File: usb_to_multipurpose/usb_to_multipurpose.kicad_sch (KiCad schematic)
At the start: 27 parts, among them P1 USB_C_Plug_USB2.0, U1 FT232H, U2 93LC56B, U3 PM2.54-1*11, U4 PM2.54-1*11, Y1 12MHz

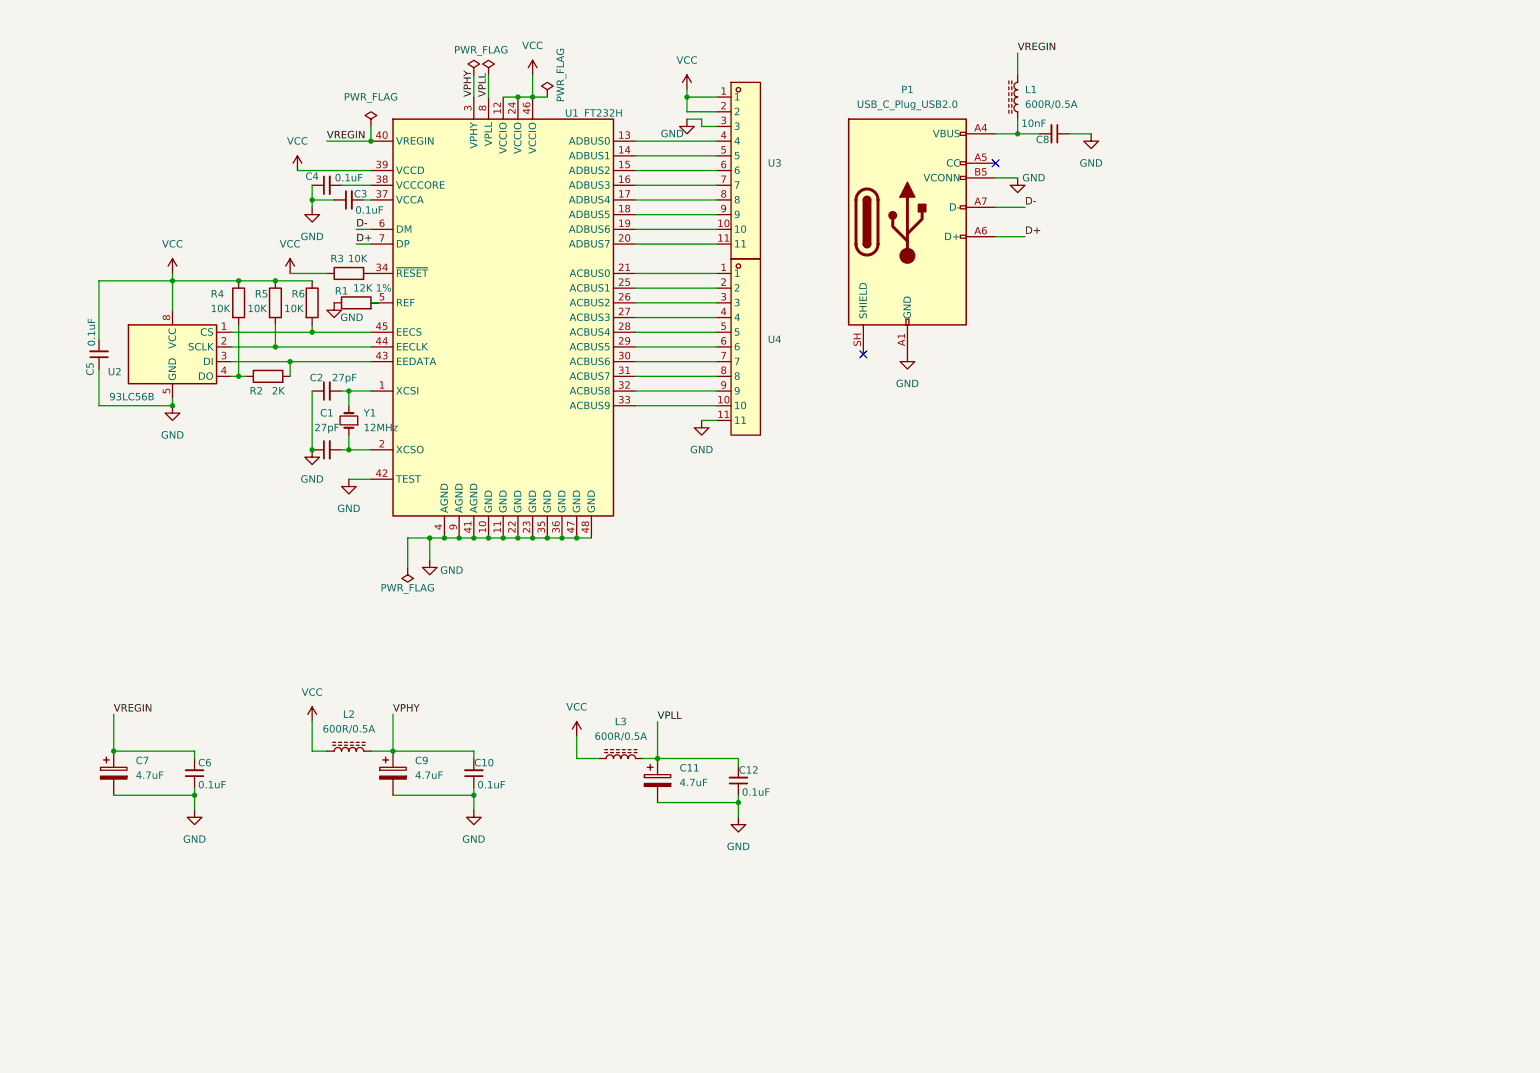
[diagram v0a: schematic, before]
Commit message: Update schematic for self-powered configuration running on 3.3V. Added footprints.
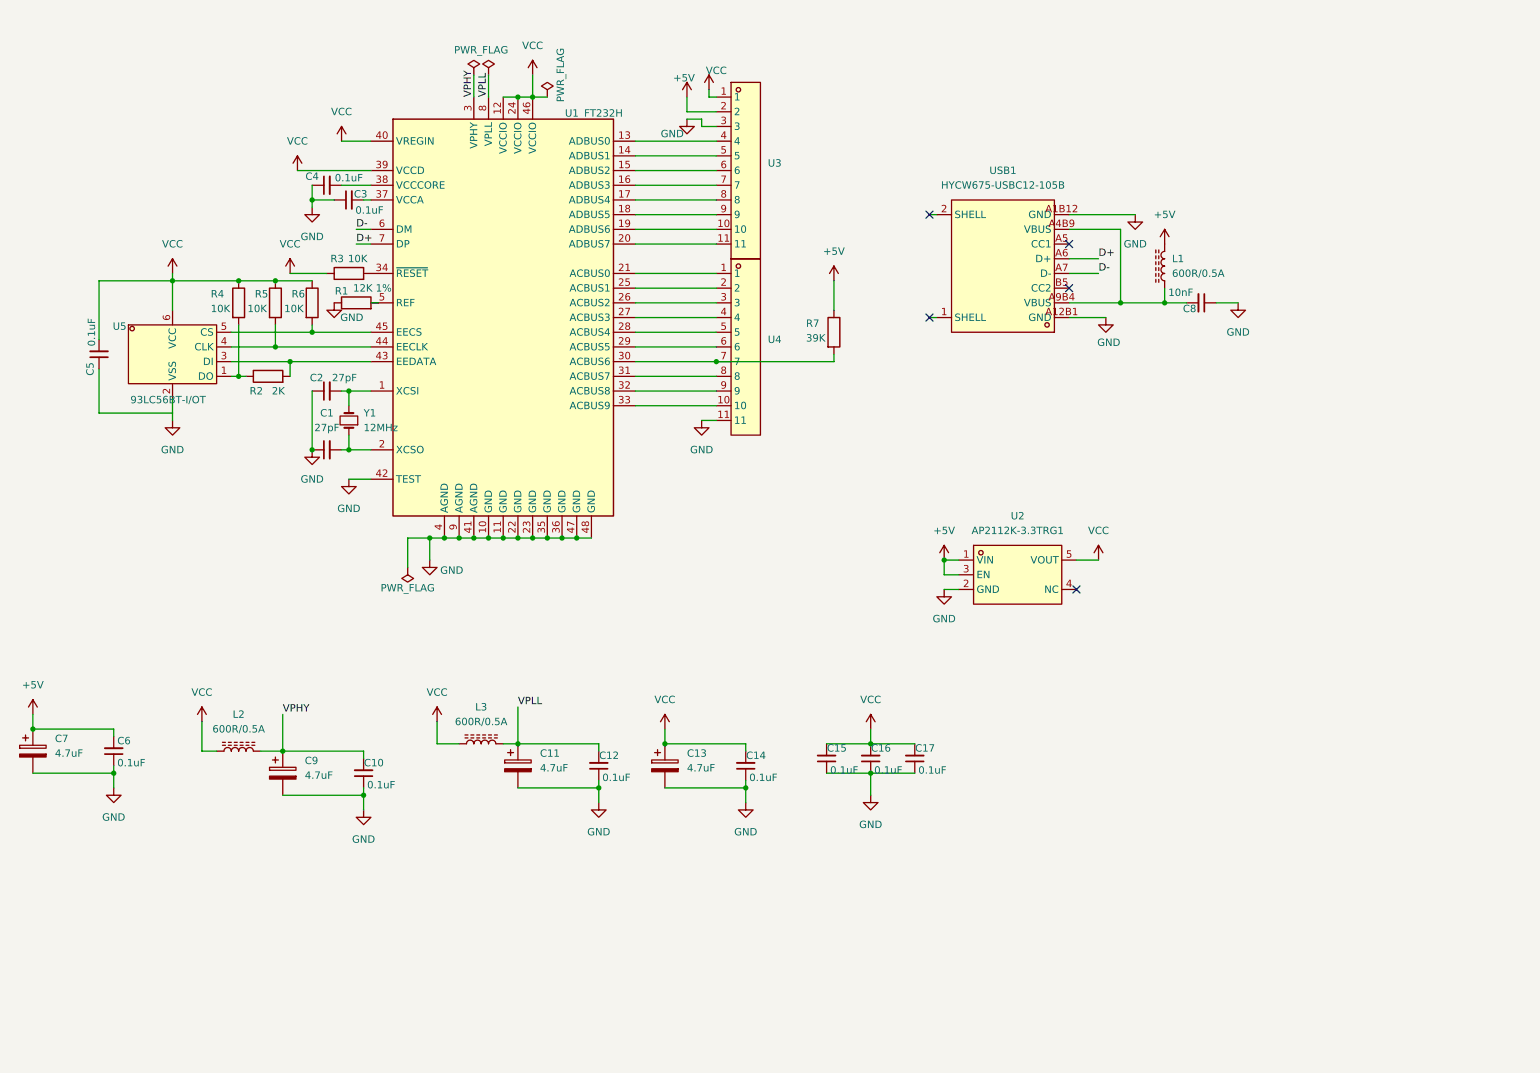
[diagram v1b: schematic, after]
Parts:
- removed P1: USB_C_Plug_USB2.0, symbol Connector:USB_C_Plug_USB2.0
- removed U2: 93LC56B, symbol Memory_EEPROM:93LCxxB
- added C13: 4.7uF, Capacitor_SMD:C_0603_1608Metric, symbol Device:C_Polarized
- added C14, C15, C16, C17: 0.1uF, Capacitor_SMD:C_0603_1608Metric, symbol Device:C_Small
- added R7: 39K, easyeda2kicad:R0402, symbol Device:R
- added U2: AP2112K-3.3TRG1, easyeda2kicad:SOT-23-5_L2.9-W1.6-P0.95-LS2.7-BR, symbol easyeda2kicad:AP2112K-3.3TRG1
- added U5: 93LC56BT-I/OT, easyeda2kicad:SOT-23-6_L2.9-W1.6-P0.95-LS2.8-BR, symbol easyeda2kicad:93LC56BT-I_OT
- added USB1: HYCW675-USBC12-105B, easyeda2kicad:USB-C-SMD_HYCW675-USBC12-105B, symbol easyeda2kicad:HYCW675-USBC12-105B
- L1, L2, L3: footprint (none) -> easyeda2kicad:L0805
- R1: footprint (none) -> easyeda2kicad:R0603
- R2, R3, R4, R5, R6: footprint (none) -> easyeda2kicad:R0402
- U1: footprint Package_DFN_QFN:QFN-48-1EP_8x8mm_P0.5mm_EP6.2x6.2mm -> easyeda2kicad:LQFP-48_L7.0-W7.0-P0.50-LS9.0-TL
- U3, U4: footprint Connector_TE-Connectivity:TE_440054-2_1x02_P2.00mm_Vertical -> easyeda2kicad:HDR-TH_11P-P2.54-V-F
- Y1: footprint Connector_TE-Connectivity:TE_440054-2_1x02_P2.00mm_Vertical -> easyeda2kicad:OSC-SMD_4P-L3.2-W2.5-BL
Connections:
- net D+: now also USB1.A6 (D+)
- net D-: now also USB1.A7 (D-)
- net GND: now also C13.2, C14.1, C15.1, C16.1, C17.1, U2.2 (GND), U5.2 (VSS), USB1.A12B1 (GND), USB1.A1B12 (GND); no longer C5.1
- net VCC: now also U1.40 (VREGIN), C13.1, C14.2, C15.2, C16.2, C17.2, U2.5 (VOUT), U5.6 (VCC); no longer U3.2
- net at U1.30 (ACBUS6), U4.7: now also R7.2
- net at R2.2, U1.43 (EEDATA): now also U5.3 (DI)
- net at R5.2, U1.44 (EECLK): now also U5.4 (CLK)
- net at R6.2, U1.45 (EECS): now also U5.5 (CS)
- net at C8.2, L1.1: now also USB1.A4B9 (VBUS), USB1.A9B4 (VBUS)
- net at R2.1, R4.2: now also U5.1 (DO)
- net VREGIN renamed +5V
- net +5V: now also U3.2, R7.1, U2.1 (VIN), U2.3 (EN); no longer U1.40 (VREGIN)
- no-connect marks 2 -> 5
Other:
- moved on the sheet: C10, C11, C12, C6, C7, C8, C9, L1, L2, L3

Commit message: Add 2*8 header. Schematic cleanup.
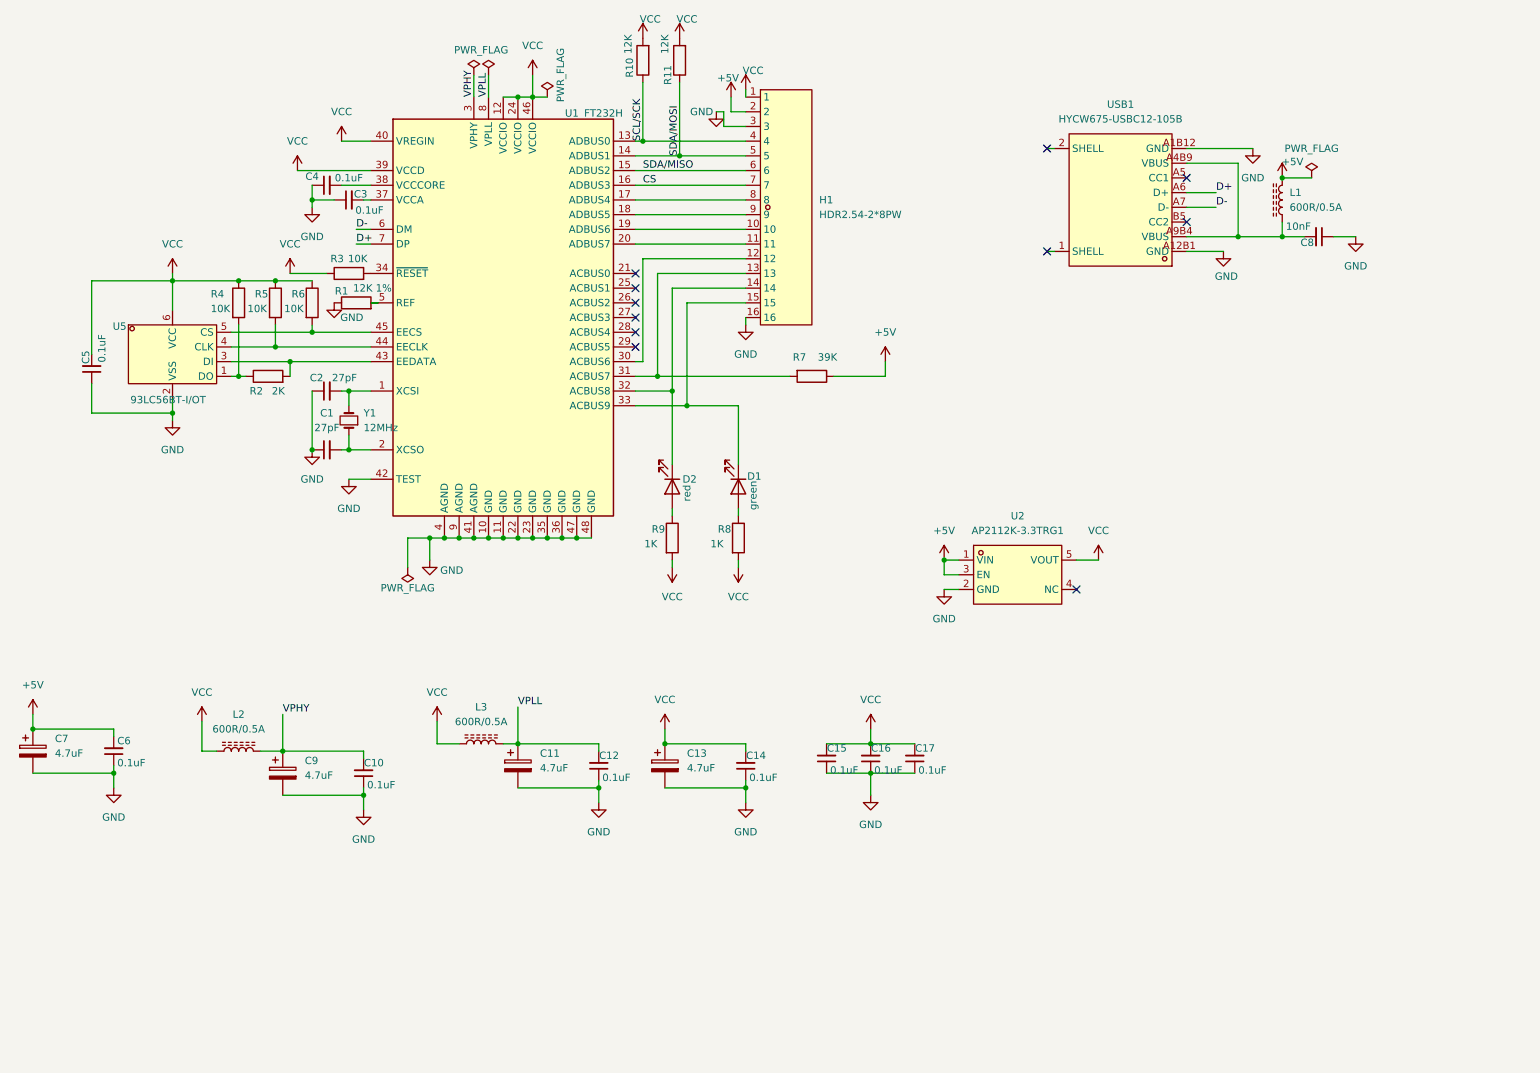
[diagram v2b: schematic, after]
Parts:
- removed U3, U4: PM2.54-1*11, easyeda2kicad:HDR-TH_11P-P2.54-V-F, symbol easyeda2kicad:PM2.54-1*11
- added D1: green, easyeda2kicad:LED0603-RD, symbol Device:LED
- added D2: red, easyeda2kicad:LED0603-RD, symbol Device:LED
- added H1: HDR2.54-2*8PW, easyeda2kicad:HDR-TH_16P-P2.54-H-F-R2-C8-S2.54-W10.0, symbol easyeda2kicad:HDR2.54-2*8PW
- added R10, R11: 12K, easyeda2kicad:R0603, symbol Device:R
- added R8, R9: 1K, easyeda2kicad:R0402, symbol Device:R
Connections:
- net +5V: now also H1.2
- net GND: now also C5.1, H1.16, H1.3
- net VCC: now also H1.1, R10.2, R11.2, R8.2, R9.2
- net SCL/SCK: now reaches U1.13 (ADBUS0)
- net SCL/SCK: now also H1.4, R10.1
- net SDA/MOSI: now reaches U1.14 (ADBUS1)
- net SDA/MOSI: now also H1.5, R11.1
- net SDA/MISO: now reaches U1.15 (ADBUS2)
- net SDA/MISO: now also H1.6
- net CS: now reaches U1.16 (ADBUS3)
- net CS: now also H1.7
- net at U1.17 (ADBUS4): now also H1.8
- net at U1.18 (ADBUS5): now also H1.9
- net at U1.19 (ADBUS6): now also H1.10
- net at U1.20 (ADBUS7): now also H1.11
- net at U1.30 (ACBUS6): now also H1.12; no longer R7.2
- net at U1.31 (ACBUS7): now also R7.2, H1.13
- net at U1.32 (ACBUS8): now also D2.1 (K), H1.14
- net at U1.33 (ACBUS9): now also D1.1 (K), H1.15
- new net: D2.2 (A), R9.1
- new net: D1.2 (A), R8.1
- no-connect marks 5 -> 11
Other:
- moved on the sheet: C8, L1, R7, USB1

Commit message: Schematic refinements. Add schematic info.
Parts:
- removed C13, C7: 4.7uF, Capacitor_SMD:C_0603_1608Metric, symbol Device:C_Polarized
- removed C14, C5, C6: 0.1uF, Capacitor_SMD:C_0603_1608Metric, symbol Device:C_Small
- removed R6: 10K, easyeda2kicad:R0402, symbol Device:R
- R4, R5: value 10K -> 5K1; footprint easyeda2kicad:R0402 -> (none)
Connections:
- net +5V: now also U1.40 (VREGIN)
- net GND: now also R4.2, R5.2
- net VCC: no longer R4.1, R5.1, U1.40 (VREGIN)
- net at R2.1, U5.1 (DO): no longer R4.2
- net at U1.44 (EECLK), U5.4 (CLK): no longer R5.2
- net at U1.29 (ACBUS5): now also H1.12
- net at U1.30 (ACBUS6): now also H1.13; no longer H1.12
- net at R7.2, U1.31 (ACBUS7): no longer H1.13
- net at USB1.A5 (CC1): now also R4.1
- net at USB1.B5 (CC2): now also R5.1
- no-connect marks 11 -> 8
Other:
- title: (none) -> USB to multipurpose
- moved on the sheet: C15, C16, C17, C8, L1

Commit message: Prepare v1.0 of the PCB.
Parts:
- C1, C11, C2, C9: footprint Capacitor_SMD:C_0603_1608Metric -> easyeda2kicad:C0402
- C10, C12, C15, C16, C17, C3, C4, C8: footprint Capacitor_SMD:C_0603_1608Metric -> easyeda2kicad:C0201
- R4, R5: footprint (none) -> easyeda2kicad:R0402
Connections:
- net GND: now also USB1.1 (SHELL), USB1.2 (SHELL)
- net at U1.18 (ADBUS5): now also H1.10; no longer H1.9
- net at U1.19 (ADBUS6): now also H1.9; no longer H1.10
- no-connect marks 8 -> 6
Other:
- note added: "v1.0"
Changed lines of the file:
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@@
 		(date "2026-09-06")
 	)
+	(text "v1.0"
+		(exclude_from_sim no)
+		(at 270.51 193.548 0)
+		(effects
+			(font
+				(size 1.27 1.27)
+			)
+		)
+	)
+	(text ""
+		(exclude_from_sim no)
+		(at 188.976 173.99 0)
+		(effects
+			(font
+				(size 2.54 2.54)
+			)
+		)
+	)
 	(junction
 		(at 134.62 38.1)
@@
 	)
 	(junction
+		(at 194.31 54.61)
+		(diameter 0)
+		(color 0 0 0 0)
+	)
+	(junction
 		(at 106.68 27.94)
 		(diameter 0)
@@
 	)
 	(no_connect
-		(at 198.12 54.61)
-	)
-	(no_connect
 		(at 127 66.04)
 	)
@@
 	)
 	(no_connect
-		(at 198.12 36.83)
-	)
-	(no_connect
 		(at 127 68.58)
 	)
@@
 	(wire
 		(pts
-			(xy 104.14 139.7) (xy 106.68 139.7)
+			(xy 194.31 54.61) (xy 199.39 54.61)
 		)
 		(stroke
@@
 	(wire
 		(pts
-			(xy 111.76 104.14) (xy 109.22 104.14)
+			(xy 104.14 139.7) (xy 106.68 139.7)
 		)
 		(stroke
@@
 	(wire
 		(pts
-			(xy 78.74 50.8) (xy 81.28 50.8)
+			(xy 111.76 104.14) (xy 109.22 104.14)
 		)
 		(stroke
@@
 	(wire
 		(pts
-			(xy 135.89 81.28) (xy 135.89 63.5)
+			(xy 78.74 50.8) (xy 81.28 50.8)
 		)
 		(stroke
@@
 	(wire
 		(pts
-			(xy 144.78 107.95) (xy 144.78 109.22)
+			(xy 135.89 81.28) (xy 135.89 63.5)
 		)
 		(stroke
@@
 	(wire
 		(pts
-			(xy 198.12 54.61) (xy 199.39 54.61)
+			(xy 144.78 107.95) (xy 144.78 109.22)
 		)
 		(stroke
@@
 	(wire
 		(pts
-			(xy 127 48.26) (xy 146.05 48.26)
-		)
-		(stroke
-			(width 0)
-			(type default)
-		)
-	)
-	(wire
-		(pts
 			(xy 78.74 53.34) (xy 81.28 53.34)
 		)
@@
 	(wire
 		(pts
+			(xy 127 48.26) (xy 137.16 48.26)
+		)
+		(stroke
+			(width 0)
+			(type default)
+		)
+	)
+	(wire
+		(pts
 			(xy 144.78 81.28) (xy 135.89 81.28)
 		)
@@
 	(wire
 		(pts
+			(xy 127 50.8) (xy 127 49.53)
+		)
+		(stroke
+			(width 0)
+			(type default)
+		)
+	)
+	(wire
+		(pts
 			(xy 71.12 78.74) (xy 71.12 88.9)
 		)
@@
 	(wire
 		(pts
-			(xy 127 50.8) (xy 146.05 50.8)
+			(xy 143.51 27.94) (xy 143.51 30.48)
 		)
 		(stroke
@@
 	(wire
 		(pts
-			(xy 143.51 27.94) (xy 143.51 30.48)
+			(xy 93.98 104.14) (xy 91.44 104.14)
 		)
 		(stroke
@@
 	(wire
 		(pts
-			(xy 93.98 104.14) (xy 91.44 104.14)
+			(xy 203.2 107.95) (xy 207.01 107.95)
 		)
 		(stroke
@@
 	(wire
 		(pts
-			(xy 203.2 107.95) (xy 207.01 107.95)
+			(xy 222.25 44.45) (xy 224.79 44.45)
 		)
 		(stroke
@@
 	(wire
 		(pts
-			(xy 222.25 44.45) (xy 224.79 44.45)
+			(xy 137.16 48.26) (xy 137.16 50.8)
 		)
 		(stroke
@@
 	(wire
 		(pts
+			(xy 194.31 36.83) (xy 199.39 36.83)
+		)
+		(stroke
+			(width 0)
+			(type default)
+		)
+	)
+	(wire
+		(pts
 			(xy 246.38 41.91) (xy 251.46 41.91)
 		)
@@
 	(wire
 		(pts
-			(xy 198.12 36.83) (xy 199.39 36.83)
+			(xy 246.38 49.53) (xy 246.38 52.07)
 		)
 		(stroke
@@
 	(wire
 		(pts
-			(xy 246.38 49.53) (xy 246.38 52.07)
+			(xy 130.81 58.42) (xy 130.81 73.66)
 		)
 		(stroke
@@
 	(wire
 		(pts
-			(xy 130.81 58.42) (xy 130.81 73.66)
+			(xy 120.65 140.97) (xy 120.65 139.7)
 		)
 		(stroke
@@
 	(wire
 		(pts
-			(xy 120.65 140.97) (xy 120.65 139.7)
+			(xy 194.31 36.83) (xy 194.31 54.61)
 		)
 		(stroke
@@
 	(wire
 		(pts
+			(xy 146.05 49.53) (xy 146.05 48.26)
+		)
+		(stroke
+			(width 0)
+			(type default)
+		)
+	)
+	(wire
+		(pts
 			(xy 128.27 35.56) (xy 146.05 35.56)
 		)
@@
 	(wire
 		(pts
+			(xy 137.16 50.8) (xy 146.05 50.8)
+		)
+		(stroke
+			(width 0)
+			(type default)
+		)
+	)
+	(wire
+		(pts
 			(xy 134.62 38.1) (xy 134.62 25.4)
 		)
@@
 	(wire
 		(pts
+			(xy 127 49.53) (xy 146.05 49.53)
+		)
+		(stroke
+			(width 0)
+			(type default)
+		)
+	)
+	(wire
+		(pts
 			(xy 96.52 104.14) (xy 93.98 104.14)
 		)
@@
 			)
 		)
-		(property "Footprint" "Capacitor_SMD:C_0603_1608Metric"
+		(property "Footprint" "easyeda2kicad:C0201"
 			(at 120.65 143.51 0)
 			(hide yes)
@@
 	(symbol
 		(lib_id "power:GND")
+		(at 194.31 54.61 0)
+		(unit 1)
+		(body_style 1)
+		(exclude_from_sim no)
+		(in_bom yes)
+		(on_board yes)
+		(in_pos_files yes)
+		(dnp no)
+		(property "Reference" "#PWR027"
+			(at 194.31 60.96 0)
+			(hide yes)
+			(show_name no)
+			(do_not_autoplace no)
+			(effects
+				(font
+					(size 1.27 1.27)
+				)
+			)
+		)
+		(property "Value" "GND"
+			(at 194.818 58.928 0)
+			(show_name no)
+			(do_not_autoplace no)
+			(effects
+				(font
+					(size 1.27 1.27)
+				)
+			)
+		)
+		(property "Footprint" ""
+			(at 194.31 54.61 0)
+			(hide yes)
+			(show_name no)
+			(do_not_autoplace no)
+			(effects
+				(font
+					(size 1.27 1.27)
+				)
+			)
+		)
+		(property "Datasheet" ""
+			(at 194.31 54.61 0)
+			(hide yes)
+			(show_name no)
+			(do_not_autoplace no)
+			(effects
+				(font
+					(size 1.27 1.27)
+				)
+			)
+		)
+		(property "Description" "Power symbol creates a global label with name \"GND\" , ground"
+			(at 194.31 54.61 0)
+			(hide yes)
+			(show_name no)
+			(do_not_autoplace no)
+			(effects
+				(font
+					(size 1.27 1.27)
+				)
+			)
+		)
+		(pin "1"
+		)
+		(instances
+			(project "usb_to_multipurpose"
+				(path "/562f4026-a780-4e62-b45e-c24d64d1112c"
+					(reference "#PWR027")
+					(unit 1)
+				)
+			)
+		)
+	)
+	(symbol
+		(lib_id "power:GND")
 		(at 140.97 30.48 0)
 		(unit 1)
@@
 			)
 		)
-		(property "Footprint" "Capacitor_SMD:C_0603_1608Metric"
+		(property "Footprint" "easyeda2kicad:C0402"
 			(at 67.0052 148.59 0)
 			(hide yes)
@@
 			)
 		)
-		(property "Footprint" ""
+		(property "Footprint" "easyeda2kicad:R0402"
 			(at 229.87 51.308 90)
 			(hide yes)
@@
 			)
 		)
-		(property "Footprint" "Capacitor_SMD:C_0603_1608Metric"
+		(property "Footprint" "easyeda2kicad:C0402"
 			(at 73.66 88.9 0)
 			(hide yes)
@@
 			)
 		)
-		(property "Footprint" "Capacitor_SMD:C_0603_1608Metric"
+		(property "Footprint" "easyeda2kicad:C0201"
 			(at 73.66 43.18 0)
 			(hide yes)
@@
 			)
 		)
-		(property "Footprint" "Capacitor_SMD:C_0603_1608Metric"
+		(property "Footprint" "easyeda2kicad:C0201"
 			(at 135.89 142.24 0)
 			(hide yes)
@@
 			)
 		)
-		(property "Footprint" "Capacitor_SMD:C_0603_1608Metric"
+		(property "Footprint" "easyeda2kicad:C0201"
 			(at 77.47 45.72 0)
 			(hide yes)
@@
 			)
 		)
-		(property "Footprint" "Capacitor_SMD:C_0603_1608Metric"
+		(property "Footprint" "easyeda2kicad:C0402"
 			(at 73.66 78.74 0)
 			(hide yes)
@@
 			)
 		)
-		(property "Footprint" ""
+		(property "Footprint" "easyeda2kicad:R0402"
 			(at 229.87 43.688 90)
 			(hide yes)
@@
 			)
 		)
-		(property "Footprint" "Capacitor_SMD:C_0603_1608Metric"
+		(property "Footprint" "easyeda2kicad:C0201"
 			(at 80.01 144.78 0)
 			(hide yes)
@@
 			)
 		)
-		(property "Footprint" "Capacitor_SMD:C_0603_1608Metric"
+		(property "Footprint" "easyeda2kicad:C0201"
 			(at 143.51 142.24 0)
 			(hide yes)
@@
 			)
 		)
-		(property "Footprint" "Capacitor_SMD:C_0603_1608Metric"
+		(property "Footprint" "easyeda2kicad:C0402"
 			(at 107.6452 147.32 0)
 			(hide yes)
@@
 			)
 		)
-		(property "Footprint" "Capacitor_SMD:C_0603_1608Metric"
+		(property "Footprint" "easyeda2kicad:C0201"
 			(at 252.73 52.07 0)
 			(hide yes)
@@
 			)
 		)
-		(property "Footprint" "Capacitor_SMD:C_0603_1608Metric"
+		(property "Footprint" "easyeda2kicad:C0201"
 			(at 151.13 142.24 0)
 			(hide yes)
